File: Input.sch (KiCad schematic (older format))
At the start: 13 parts, among them SW4 SW_Push, U2 BNO055, U4 BMP280

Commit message: rc and cont on pyro, linear reg, flash
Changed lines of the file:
@@
 Wire Notes Line
 	6550 5700 6550 5200
-Text Notes 6125 1700 0    118  ~ 24
+Text Notes 4625 1775 0    118  ~ 24
 INPUT
 Text Notes 4675 3925 0    39   ~ 0

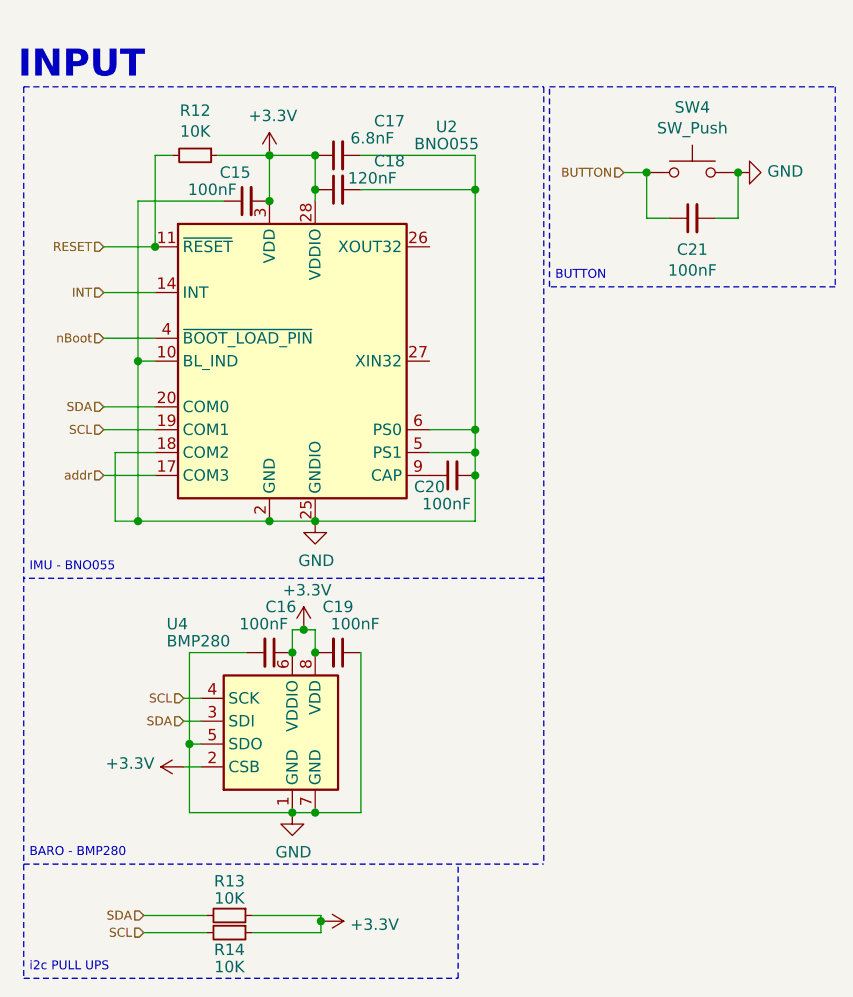
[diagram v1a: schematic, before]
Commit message: bno055 removed, bmi088, schotksy
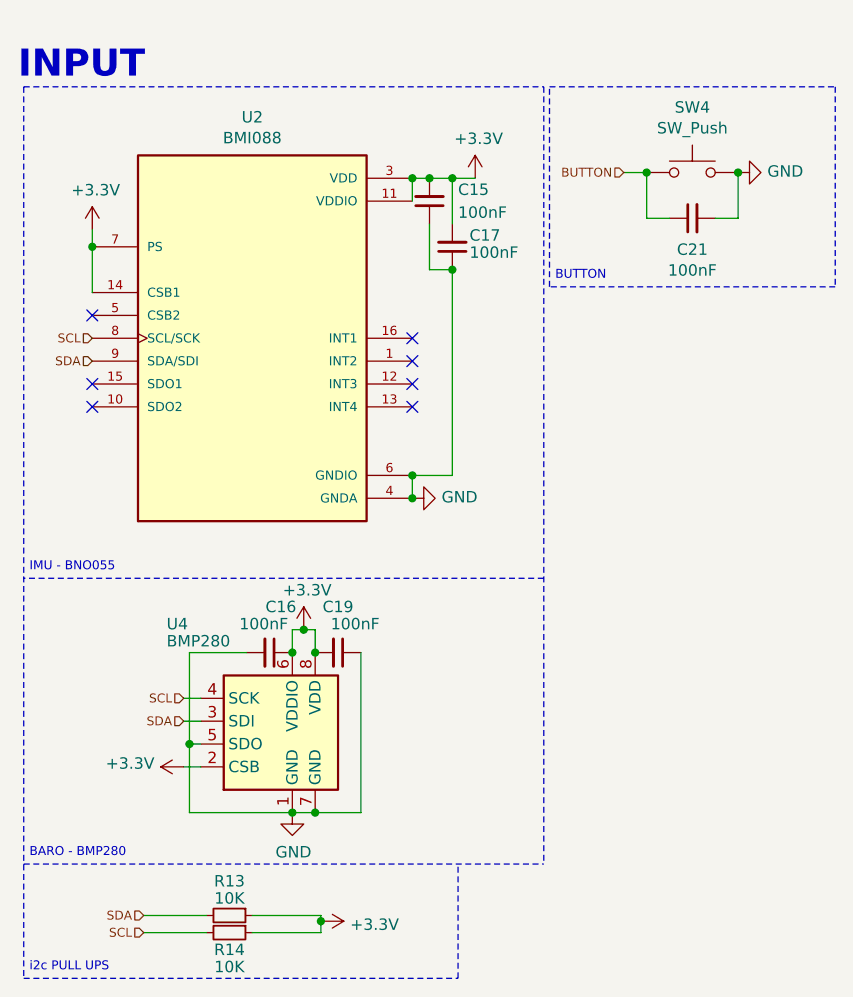
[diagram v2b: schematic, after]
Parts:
- removed C18: 120nF, Capacitor_SMD:C_0603_1608Metric, symbol Device:C_Small
- removed C20: 100nF, Capacitor_SMD:C_0603_1608Metric, symbol Device:C_Small
- removed R12: 10K, Capacitor_SMD:C_0603_1608Metric, symbol Device:R_Small
- removed U2: BNO055, Package_LGA:LGA-28_5.2x3.8mm_P0.5mm, symbol Sensor_Motion:BNO055
- added U2: BMI088, BMI088:PQFN50P450X300X100-16N, symbol BMI088:BMI088
- C17: value 6.8nF -> 100nF
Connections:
- net +3V3: now also C17.2, U2.11 (VDDIO), U2.14 (CSB1), U2.3 (VDD), U2.7 (PS); no longer C17.1
- net GND: now also C17.1, U2.4 (GNDA), U2.6 (GNDIO); no longer C17.2
- net SCL: now also U2.8 (SCL/SCK)
- net SDA: now also U2.9 (SDA/SDI)
- no-connect marks 0 -> 7

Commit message: Schematic cleanup, pyro
thanks ben for the advice
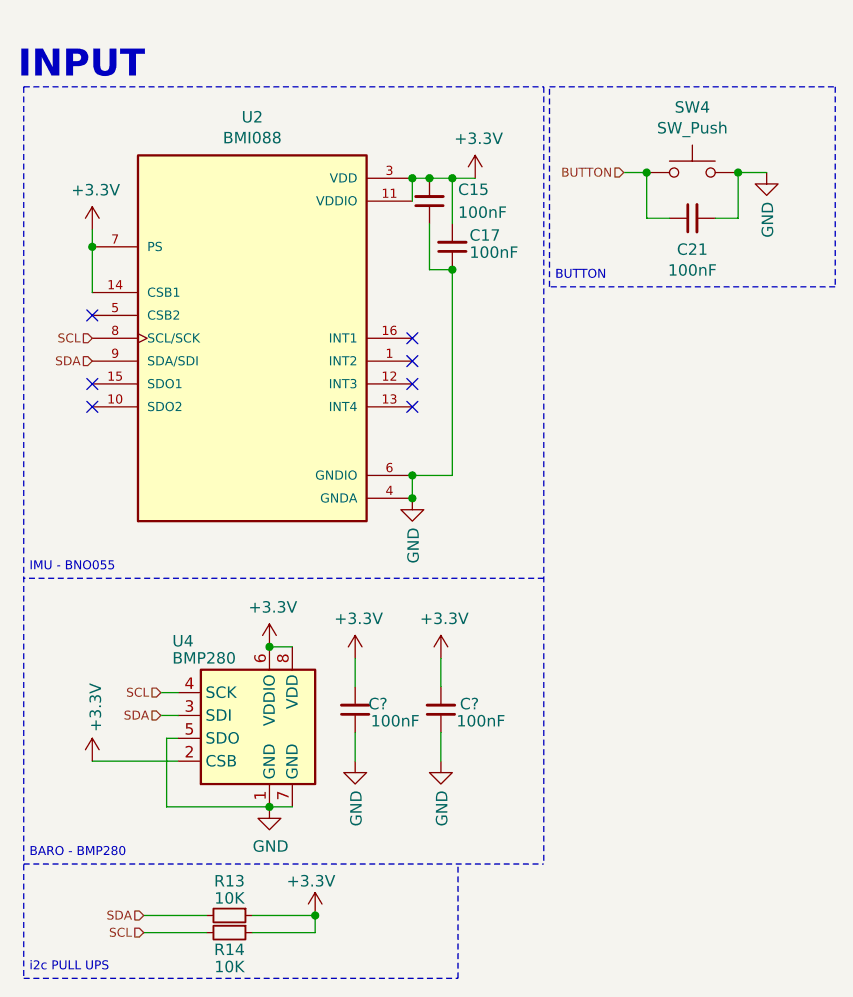
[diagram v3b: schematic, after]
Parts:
- removed C16, C19: 100nF, Capacitor_SMD:C_0603_1608Metric, symbol Device:C_Small
- added C? (x2): 100nF, Capacitor_SMD:C_0603_1608Metric, symbol Device:C_Small
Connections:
- net +3V3: now also C?.2, C?.2
- net GND: now also C?.1, C?.1
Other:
- moved on the sheet: U4

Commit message: more cleanup
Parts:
- R13, R14: footprint Capacitor_SMD:C_0603_1608Metric -> Resistor_SMD:R_0603_1608Metric
- gave numbers to parts that had none: 2
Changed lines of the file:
@@
 $Descr A4 11693 8268
 encoding utf-8
-Sheet 3 3
+Sheet 2 3
 Title ""
 Date ""
@@
 P 6350 3600
 F 0 "#PWR0129" H 6350 3350 50  0001 C CNN
-F 1 "GND" V 6355 3472 50  0000 R CNN
+F 1 "GND" H 6425 3450 50  0000 R CNN
 F 2 "" H 6350 3600 50  0001 C CNN
 F 3 "" H 6350 3600 50  0001 C CNN
@@
 P 6625 2200
 F 0 "#PWR0130" H 6625 2050 50  0001 C CNN
-F 1 "+3.3V" H 6640 2373 50  0000 C CNN
+F 1 "+3.3V" H 6600 2350 50  0000 C CNN
 F 2 "" H 6625 2200 50  0001 C CNN
 F 3 "" H 6625 2200 50  0001 C CNN
@@
 P 4950 2425
 F 0 "#PWR0132" H 4950 2275 50  0001 C CNN
-F 1 "+3.3V" H 4965 2598 50  0000 C CNN
+F 1 "+3.3V" H 4925 2575 50  0000 C CNN
 F 2 "" H 4950 2425 50  0001 C CNN
 F 3 "" H 4950 2425 50  0001 C CNN
@@
 AR Path="/604A6029/604AB796" Ref="#PWR0138"  Part="1"
 F 0 "#PWR0138" H 7900 1925 50  0001 C CNN
-F 1 "GND" V 7905 2047 50  0000 R CNN
+F 1 "GND" H 7975 2025 50  0000 R CNN
 F 2 "" H 7900 2175 50  0001 C CNN
 F 3 "" H 7900 2175 50  0001 C CNN
@@
 U 1 1 6055E63E
 P 6100 4525
-F 0 "C?" H 6000 4500 50  0000 C CNN
+AR Path="/604AFA5F/6055E63E" Ref="C?"  Part="1"
+AR Path="/604A6029/6055E63E" Ref="C12"  Part="1"
+F 0 "C12" H 6000 4500 50  0000 C CNN
 F 1 "100nF" H 5925 4575 50  0000 C CNN
 F 2 "Capacitor_SMD:C_0603_1608Metric" H 6100 4525 50  0001 C CNN
@@
 U 1 1 6055E644
 P 6100 4300
-F 0 "#PWR?" H 6100 4150 50  0001 C CNN
-F 1 "+3.3V" H 6115 4473 50  0000 C CNN
+AR Path="/604AFA5F/6055E644" Ref="#PWR?"  Part="1"
+AR Path="/604A6029/6055E644" Ref="#PWR0128"  Part="1"
+F 0 "#PWR0128" H 6100 4150 50  0001 C CNN
+F 1 "+3.3V" H 6075 4450 50  0000 C CNN
 F 2 "" H 6100 4300 50  0001 C CNN
 F 3 "" H 6100 4300 50  0001 C CNN
@@
 U 1 1 6055E64A
 P 6100 4750
-F 0 "#PWR?" H 6100 4500 50  0001 C CNN
-F 1 "GND" V 6105 4622 50  0000 R CNN
+AR Path="/604AFA5F/6055E64A" Ref="#PWR?"  Part="1"
+AR Path="/604A6029/6055E64A" Ref="#PWR0133"  Part="1"
+F 0 "#PWR0133" H 6100 4500 50  0001 C CNN
+F 1 "GND" H 6175 4600 50  0000 R CNN
 F 2 "" H 6100 4750 50  0001 C CNN
 F 3 "" H 6100 4750 50  0001 C CNN
@@
 U 1 1 6056477B
 P 6475 4525
-F 0 "C?" H 6350 4500 50  0000 C CNN
+AR Path="/604AFA5F/6056477B" Ref="C?"  Part="1"
+AR Path="/604A6029/6056477B" Ref="C13"  Part="1"
+F 0 "C13" H 6350 4500 50  0000 C CNN
 F 1 "100nF" H 6300 4575 50  0000 C CNN
 F 2 "Capacitor_SMD:C_0603_1608Metric" H 6475 4525 50  0001 C CNN
@@
 U 1 1 60564781
 P 6475 4300
-F 0 "#PWR?" H 6475 4150 50  0001 C CNN
-F 1 "+3.3V" H 6490 4473 50  0000 C CNN
+AR Path="/604AFA5F/60564781" Ref="#PWR?"  Part="1"
+AR Path="/604A6029/60564781" Ref="#PWR0149"  Part="1"
+F 0 "#PWR0149" H 6475 4150 50  0001 C CNN
+F 1 "+3.3V" H 6450 4450 50  0000 C CNN
 F 2 "" H 6475 4300 50  0001 C CNN
 F 3 "" H 6475 4300 50  0001 C CNN
@@
 U 1 1 60564787
 P 6475 4750
-F 0 "#PWR?" H 6475 4500 50  0001 C CNN
-F 1 "GND" V 6480 4622 50  0000 R CNN
+AR Path="/604AFA5F/60564787" Ref="#PWR?"  Part="1"
+AR Path="/604A6029/60564787" Ref="#PWR0150"  Part="1"
+F 0 "#PWR0150" H 6475 4500 50  0001 C CNN
+F 1 "GND" H 6550 4600 50  0000 R CNN
 F 2 "" H 6475 4750 50  0001 C CNN
 F 3 "" H 6475 4750 50  0001 C CNN
@@
 AR Path="/604A6029/6048228E" Ref="#PWR0137"  Part="1"
 F 0 "#PWR0137" H 4950 4600 50  0001 C CNN
-F 1 "+3.3V" V 4965 4878 50  0000 L CNN
+F 1 "+3.3V" H 4800 4900 50  0000 L CNN
 F 2 "" H 4950 4750 50  0001 C CNN
 F 3 "" H 4950 4750 50  0001 C CNN
@@
 AR Path="/604A6029/60482274" Ref="#PWR0135"  Part="1"
 F 0 "#PWR0135" H 5725 4100 50  0001 C CNN
-F 1 "+3.3V" H 5740 4423 50  0000 C CNN
+F 1 "+3.3V" H 5700 4400 50  0000 C CNN
 F 2 "" H 5725 4250 50  0001 C CNN
 F 3 "" H 5725 4250 50  0001 C CNN
@@
 F 0 "R14" V 5625 5500 50  0000 C CNN
 F 1 "10K" V 5700 5500 50  0000 C CNN
-F 2 "Capacitor_SMD:C_0603_1608Metric" H 5550 5500 50  0001 C CNN
+F 2 "Resistor_SMD:R_0603_1608Metric" H 5550 5500 50  0001 C CNN
 F 3 "~" H 5550 5500 50  0001 C CNN
 	1    5550 5500
@@
 F 0 "R13" V 5400 5425 50  0000 C CNN
 F 1 "10K" V 5475 5425 50  0000 C CNN
-F 2 "Capacitor_SMD:C_0603_1608Metric" H 5550 5425 50  0001 C CNN
+F 2 "Resistor_SMD:R_0603_1608Metric" H 5550 5425 50  0001 C CNN
 F 3 "~" H 5550 5425 50  0001 C CNN
 	1    5550 5425

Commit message: MOAR CLEANUP
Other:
- note added: "IMU - BMI088\n"
- note removed: "IMU - BNO055"
- moved on the sheet: C13
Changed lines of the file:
@@
 $Descr A4 11693 8268
 encoding utf-8
-Sheet 2 3
+Sheet 3 3
 Title ""
 Date ""
@@
 Text Notes 4625 1775 0    118  ~ 24
 INPUT
-Text Notes 4675 3925 0    39   ~ 0
-IMU - BNO055
 Text Notes 4675 5175 0    39   ~ 0
 BARO - BMP280\n
@@
 U 1 1 6061D6E6
 P 6425 2300
-F 0 "C15" H 6300 2250 50  0000 R CNN
+F 0 "C15" H 6300 2275 50  0000 R CNN
 F 1 "100nF" H 6300 2350 50  0000 R CNN
 F 2 "Capacitor_SMD:C_0603_1608Metric" H 6425 2300 50  0001 C CNN
@@
 AR Path="/604AFA5F/6055E63E" Ref="C?"  Part="1"
 AR Path="/604A6029/6055E63E" Ref="C12"  Part="1"
-F 0 "C12" H 6000 4500 50  0000 C CNN
-F 1 "100nF" H 5925 4575 50  0000 C CNN
+F 0 "C12" H 5950 4500 50  0000 C CNN
+F 1 "100nF" H 5900 4575 50  0000 C CNN
 F 2 "Capacitor_SMD:C_0603_1608Metric" H 6100 4525 50  0001 C CNN
 F 3 "~" H 6100 4525 50  0001 C CNN
@@
 L Device:C_Small C?
 U 1 1 6056477B
-P 6475 4525
+P 6500 4525
 AR Path="/604AFA5F/6056477B" Ref="C?"  Part="1"
 AR Path="/604A6029/6056477B" Ref="C13"  Part="1"
 F 0 "C13" H 6350 4500 50  0000 C CNN
 F 1 "100nF" H 6300 4575 50  0000 C CNN
-F 2 "Capacitor_SMD:C_0603_1608Metric" H 6475 4525 50  0001 C CNN
-F 3 "~" H 6475 4525 50  0001 C CNN
-	1    6475 4525
+F 2 "Capacitor_SMD:C_0603_1608Metric" H 6500 4525 50  0001 C CNN
+F 3 "~" H 6500 4525 50  0001 C CNN
+	1    6500 4525
 	-1   0    0    1
 $EndComp
@@
 L power:+3.3V #PWR?
 U 1 1 60564781
-P 6475 4300
+P 6500 4300
 AR Path="/604AFA5F/60564781" Ref="#PWR?"  Part="1"
 AR Path="/604A6029/60564781" Ref="#PWR0149"  Part="1"
-F 0 "#PWR0149" H 6475 4150 50  0001 C CNN
-F 1 "+3.3V" H 6450 4450 50  0000 C CNN
-F 2 "" H 6475 4300 50  0001 C CNN
-F 3 "" H 6475 4300 50  0001 C CNN
-	1    6475 4300
+F 0 "#PWR0149" H 6500 4150 50  0001 C CNN
+F 1 "+3.3V" H 6475 4450 50  0000 C CNN
+F 2 "" H 6500 4300 50  0001 C CNN
+F 3 "" H 6500 4300 50  0001 C CNN
+	1    6500 4300
 	1    0    0    -1
 $EndComp
@@
 L power:GND #PWR?
 U 1 1 60564787
-P 6475 4750
+P 6500 4750
 AR Path="/604AFA5F/60564787" Ref="#PWR?"  Part="1"
 AR Path="/604A6029/60564787" Ref="#PWR0150"  Part="1"
-F 0 "#PWR0150" H 6475 4500 50  0001 C CNN
-F 1 "GND" H 6550 4600 50  0000 R CNN
-F 2 "" H 6475 4750 50  0001 C CNN
-F 3 "" H 6475 4750 50  0001 C CNN
-	1    6475 4750
-	1    0    0    -1
-$EndComp
-Wire Wire Line
-	6475 4750 6475 4625
-Wire Wire Line
-	6475 4425 6475 4300
+F 0 "#PWR0150" H 6500 4500 50  0001 C CNN
+F 1 "GND" H 6575 4600 50  0000 R CNN
+F 2 "" H 6500 4750 50  0001 C CNN
+F 3 "" H 6500 4750 50  0001 C CNN
+	1    6500 4750
+	1    0    0    -1
+$EndComp
+Wire Wire Line
+	6500 4750 6500 4625
+Wire Wire Line
+	6500 4425 6500 4300
 Connection ~ 5725 4250
 Wire Wire Line
@@
 	5925 5500 5925 5425
 Connection ~ 5925 5425
+Text Notes 4675 3925 0    39   ~ 0
+IMU - BMI088\n
 $EndSCHEMATC
